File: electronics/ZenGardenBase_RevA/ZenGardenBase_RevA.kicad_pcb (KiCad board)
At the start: 2 copper layers, 101.6 x 53.3 mm, 14 parts, among them P1 Digital, P10 CONN_01X01, P11 CONN_01X01, P12 CONN_01X01, P13 CONN_01X01, P2 Power, P3 Analog, P4 Analog, P5 PWM, P6 PWM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

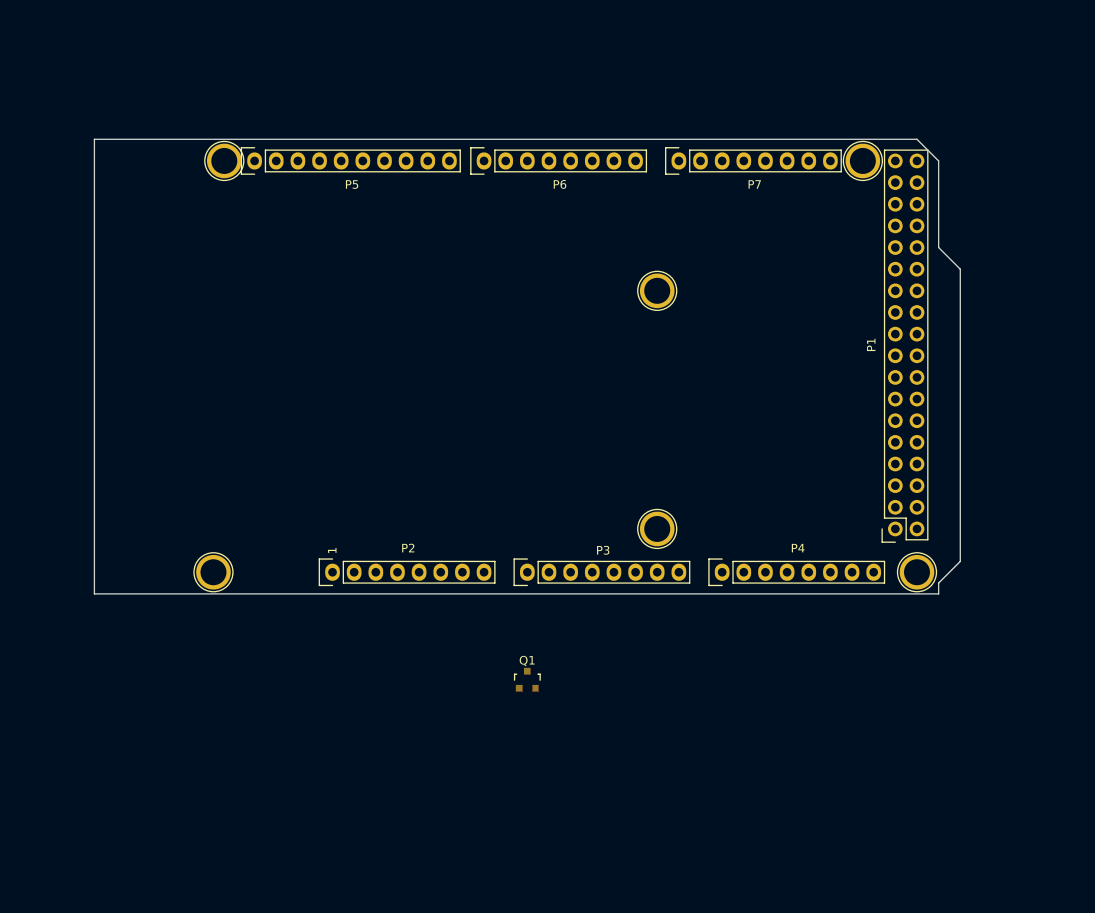
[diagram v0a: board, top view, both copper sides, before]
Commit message: updated base schematic and layout to show that it will be easier to do on a breadboard
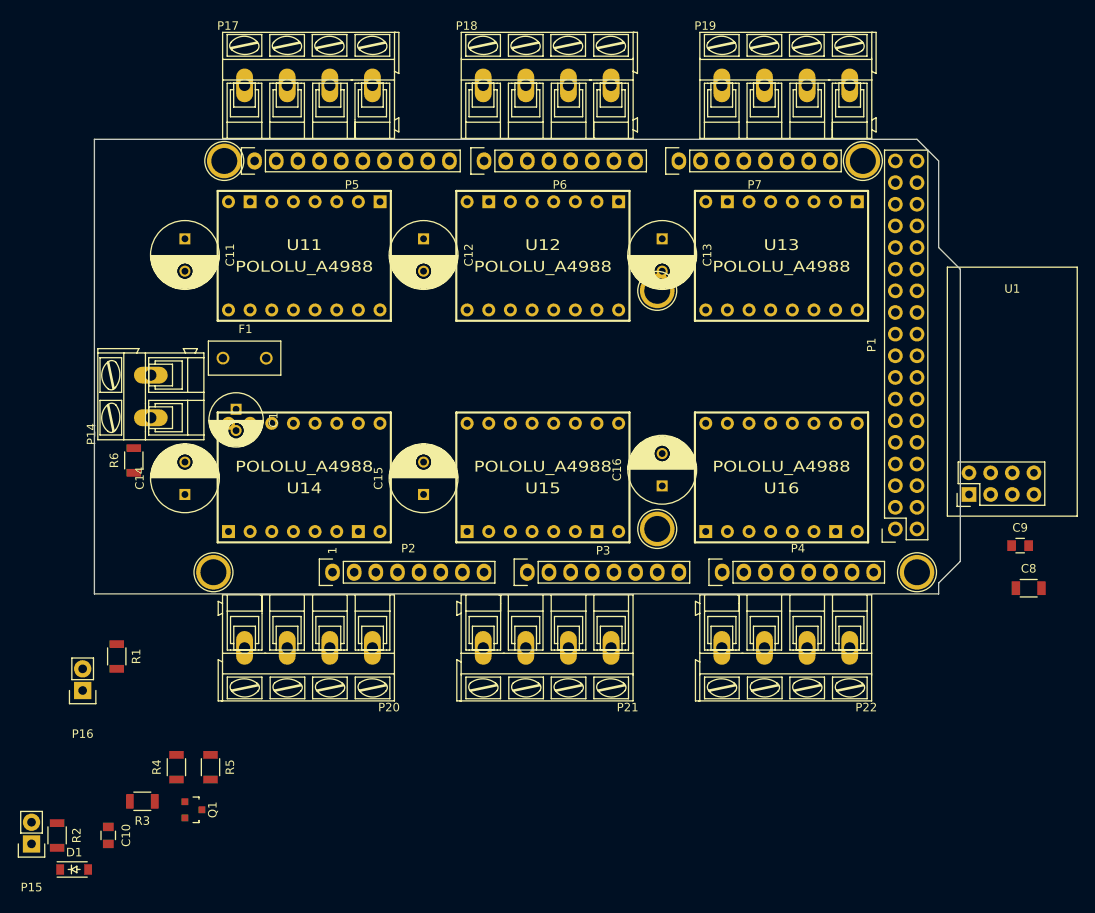
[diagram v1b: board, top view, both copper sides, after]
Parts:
- added C1: 50uF 50V, Capacitors_ThroughHole:C_Radial_D6.3_L11.2_P2.5, F.Cu at (120.0, 100.0)
- added C10: 0.1uF, Capacitors_SMD:C_0805, F.Cu at (105.0, 150.0)
- added C11: 100uF 50V, Capacitors_ThroughHole:C_Radial_D8_L13_P3.8, F.Cu at (114.0, 80.0)
- added C12: 100uF 50V, Capacitors_ThroughHole:C_Radial_D8_L13_P3.8, F.Cu at (142.0, 80.0)
- added C13: 100uF 50V, Capacitors_ThroughHole:C_Radial_D8_L13_P3.8, F.Cu at (170.0, 80.0)
- added C14: 100uF 50V, Capacitors_ThroughHole:C_Radial_D8_L13_P3.8, F.Cu at (114.0, 110.0)
- added C15: 100uF 50V, Capacitors_ThroughHole:C_Radial_D8_L13_P3.8, F.Cu at (142.0, 110.0)
- added C16: 100uF 50V, Capacitors_ThroughHole:C_Radial_D8_L13_P3.8, F.Cu at (170.0, 109.0)
- added C8: 10uF, Capacitors_SMD:C_1206, F.Cu at (213.0, 121.0)
- added C9: 0.1uF, Capacitors_SMD:C_0805, F.Cu at (212.0, 116.0)
- added D1: Diode, Diodes_SMD:SOD-123, F.Cu at (101.0, 154.0)
- added F1: FUSE, Fuse_Holders_and_Fuses:Fuse_TE5_Littlefuse-395Series, F.Cu at (121.0, 94.0)
- added P14: CONN_01X02, Connect:AK300-2, F.Cu at (110.0, 101.0)
- added P15: CONN_PZ, Pin_Headers:Pin_Header_Straight_1x02, F.Cu at (96.0, 151.0)
- added P16: CONN_VSTAT, Pin_Headers:Pin_Header_Straight_1x02, F.Cu at (102.0, 133.0)
- added P17: CONN_M1, Connect:AK300-4, F.Cu at (121.0, 62.0)
- added P18: CONN_M2, Connect:AK300-4, F.Cu at (149.0, 62.0)
- added P19: CONN_M3, Connect:AK300-4, F.Cu at (177.0, 62.0)
- added P20: CONN_M4, Connect:AK300-4, F.Cu at (136.0, 128.0)
- added P21: CONN_M5, Connect:AK300-4, F.Cu at (164.0, 128.0)
- added P22: CONN_M6, Connect:AK300-4, F.Cu at (192.0, 128.0)
- added R1: 10K, Resistors_SMD:R_1206, F.Cu at (106.0, 129.0)
- added R2: 1M, Resistors_SMD:R_1206, F.Cu at (99.0, 150.0)
- added R3: 1K, Resistors_SMD:R_1206, F.Cu at (109.0, 146.0)
- added R4: 100K, Resistors_SMD:R_1206, F.Cu at (113.0, 142.0)
- added R5: 1K, Resistors_SMD:R_1206, F.Cu at (117.0, 142.0)
- added R6: 0, Resistors_SMD:R_1206, F.Cu at (108.0, 106.0)
- added U1: NRF24L01+, MyKiCadParts:NRF24L01+, F.Cu at (206.0, 110.0)
- added U11: POLOLU_A4988, MyKiCadParts:SWDIP8_.6W, F.Cu at (128.0, 82.0)
- added U12: POLOLU_A4988, MyKiCadParts:SWDIP8_.6W, F.Cu at (156.0, 82.0)
- added U13: POLOLU_A4988, MyKiCadParts:SWDIP8_.6W, F.Cu at (184.0, 82.0)
- added U14: POLOLU_A4988, MyKiCadParts:SWDIP8_.6W, F.Cu at (128.0, 108.0)
- added U15: POLOLU_A4988, MyKiCadParts:SWDIP8_.6W, F.Cu at (156.0, 108.0)
- added U16: POLOLU_A4988, MyKiCadParts:SWDIP8_.6W, F.Cu at (184.0, 108.0)
- moved Q1 42.0 mm to (115.0, 147.0), turned to 270 degrees
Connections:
- P1 pad 10: (no net) -> /47
- P1 pad 11: (no net) -> /44
- P1 pad 12: (no net) -> /45
- P1 pad 13: (no net) -> /42
- P1 pad 14: (no net) -> MEN
- P1 pad 15: (no net) -> /40
- P1 pad 16: (no net) -> MS0
- P1 pad 17: (no net) -> /38
- P1 pad 18: (no net) -> MS1
- P1 pad 19: (no net) -> /36
- P1 pad 20: (no net) -> MS2
- P1 pad 21: (no net) -> M4_STEP
- P1 pad 22: (no net) -> M1_STEP
- P1 pad 23: (no net) -> M4_DIR
- P1 pad 24: (no net) -> M1_DIR
- P1 pad 25: (no net) -> M5_STEP
- P1 pad 26: (no net) -> M2_STEP
- P1 pad 27: (no net) -> M5_DIR
- P1 pad 28: (no net) -> M2_DIR
- P1 pad 29: (no net) -> M6_STEP
- P1 pad 3: (no net) -> SCK
- P1 pad 30: (no net) -> M3_STEP
- P1 pad 31: (no net) -> M6_DIR
- P1 pad 32: (no net) -> M3_DIR
- P1 pad 33: (no net) -> /22
- P1 pad 34: (no net) -> /23
- P1 pad 4: (no net) -> CSN
- P1 pad 5: (no net) -> MISO
- P1 pad 6: (no net) -> MOSI
- P1 pad 7: (no net) -> /48
- P1 pad 8: (no net) -> CE
- P1 pad 9: (no net) -> /46
- P10 pad 1: (no net) -> Net-(P10-Pad1)
- P11 pad 1: (no net) -> Net-(P11-Pad1)
- P12 pad 1: (no net) -> Net-(P12-Pad1)
- P13 pad 1: (no net) -> Net-(P13-Pad1)
- P2 pad 1: (no net) -> Net-(P2-Pad1)
- P2 pad 2: (no net) -> /IOREF
- P2 pad 3: (no net) -> /Reset
- P2 pad 4: (no net) -> V33
- P2 pad 8: (no net) -> VRAW
- P3 pad 1: (no net) -> VSTAT
- P3 pad 2: (no net) -> PZ_0
- P3 pad 3: (no net) -> PZ_1
- P3 pad 4: (no net) -> /A3
- P3 pad 5: (no net) -> /A4
- P3 pad 6: (no net) -> /A5
- P3 pad 7: (no net) -> /A6
- P3 pad 8: (no net) -> /A7
- P4 pad 1: (no net) -> /A8
- P4 pad 2: (no net) -> /A9
- P4 pad 3: (no net) -> /A10
- P4 pad 4: (no net) -> /A11
- P4 pad 5: (no net) -> /A12
- P4 pad 6: (no net) -> /A13
- P4 pad 7: (no net) -> /A14
- P4 pad 8: (no net) -> /A15
- P5 pad 1: (no net) -> /SCL
- P5 pad 10: (no net) -> /8(**)
- P5 pad 2: (no net) -> /SDA
- P5 pad 3: (no net) -> /AREF
- P5 pad 5: (no net) -> /13(**)
- P5 pad 6: (no net) -> /12(**)
- P5 pad 7: (no net) -> /11(**)
- P5 pad 8: (no net) -> /10(**)
- P5 pad 9: (no net) -> /9(**)
- P6 pad 1: (no net) -> /7(**)
- P6 pad 2: (no net) -> /6(**)
- P6 pad 3: (no net) -> /5(**)
- P6 pad 4: (no net) -> /4(**)
- P6 pad 5: (no net) -> /3(**)
- P6 pad 6: (no net) -> /2(**)
- P6 pad 7: (no net) -> /1(Tx0)
- P6 pad 8: (no net) -> /0(Rx0)
- P7 pad 1: (no net) -> /14(Tx3)
- P7 pad 2: (no net) -> /15(Rx3)
- P7 pad 3: (no net) -> /16(Tx2)
- P7 pad 4: (no net) -> /17(Rx2)
- P7 pad 5: (no net) -> /18(Tx1)
- P7 pad 6: (no net) -> /19(Rx1)
- P7 pad 7: (no net) -> /20(SDA)
- P7 pad 8: (no net) -> /21(SCL)
- P8 pad 1: (no net) -> Net-(P8-Pad1)
- P9 pad 1: (no net) -> Net-(P9-Pad1)
- Q1 pad 1: (no net) -> Net-(Q1-Pad1)
- Q1 pad 2: (no net) -> PZ_0
- Q1 pad 3: (no net) -> PZ_1
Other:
- net class Default: clearance 0.2 -> 0.8; trace_width 0.25 -> 0.3
- rule trace_clearance: 0.2 -> 0.8
